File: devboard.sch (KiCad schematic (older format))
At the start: 95 parts, among them J1 Conn_01x04, J2 Conn_02x05_Odd_Even, J3 USB_B_Micro, J4 Conn_01x04, J5 Conn_02x10_Counter_Clockwise, J6 Conn_02x04_Counter_Clockwise, J7 Conn_02x03_Counter_Clockwise, Q1 Q_NPN_BEC, Q2 Q_NPN_BEC, SW1 SW_SPST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

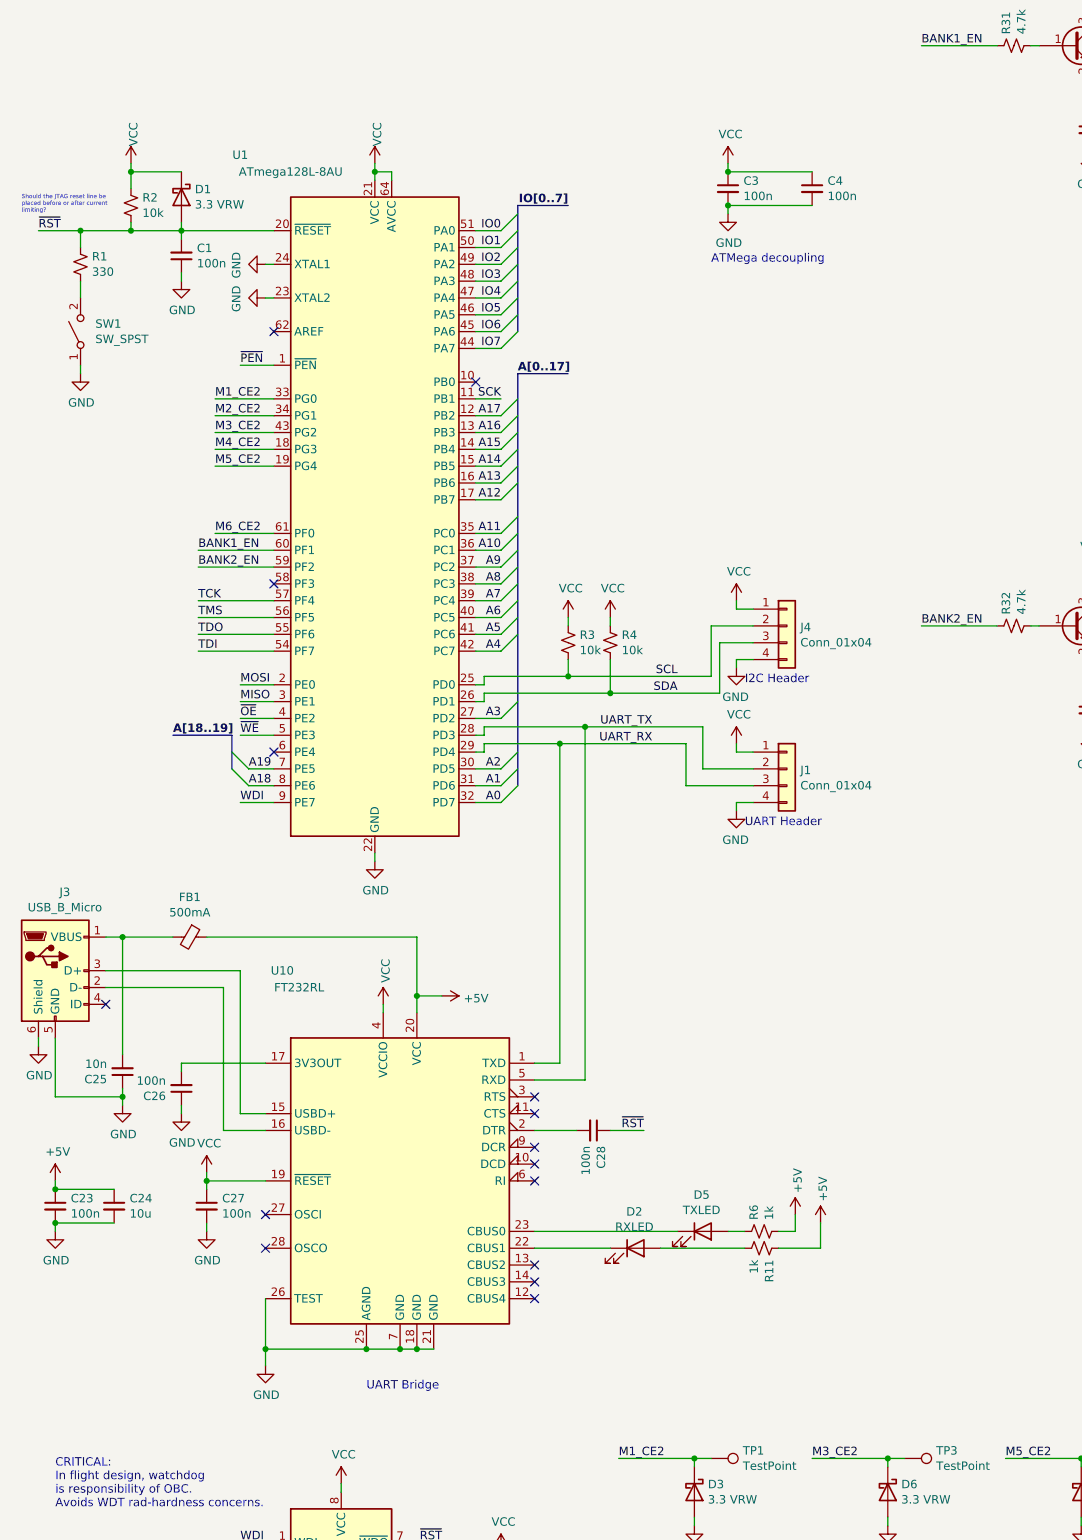
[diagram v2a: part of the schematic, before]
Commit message: Add crystal pads, MCU LED, fix serial routing
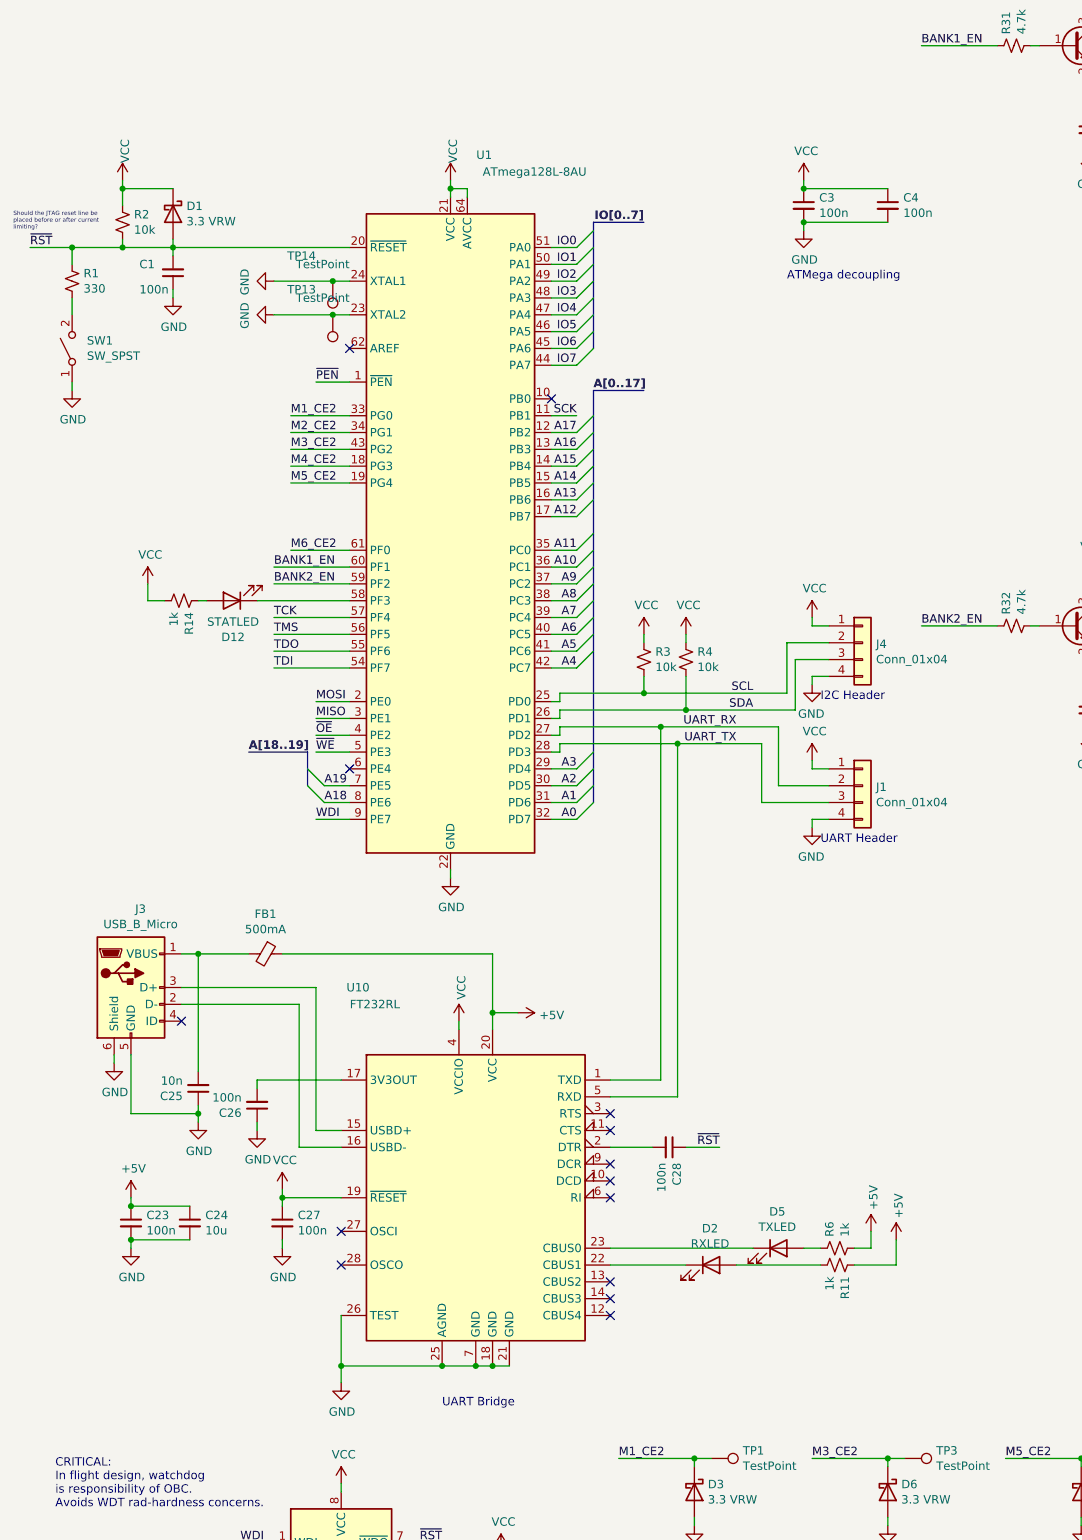
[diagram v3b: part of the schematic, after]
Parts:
- added D12: STATLED, LED_SMD:LED_0603_1608Metric_Castellated, symbol Device:LED
- added R14: 1k, Resistor_SMD:R_0603_1608Metric_Pad0.98x0.95mm_HandSolder, symbol Device:R_Small_US
- added TP13, TP14: TestPoint, TestPoint:TestPoint_Bridge_Pitch2.54mm_Drill0.7mm, symbol Connector:TestPoint
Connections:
- net A3: now also U1.29 (PD4); no longer U1.27 (PD2)
- net GND: now also TP13.1, TP14.1
- net UART_RX: now also J1.2 (Pin_2), U1.27 (PD2); no longer J1.3 (Pin_3), U1.29 (PD4)
- net UART_TX: now also J1.3 (Pin_3); no longer J1.2 (Pin_2)
- net VCC: now also R14.2
- net at U1.58 (PF3): now also D12.1 (K)
- new net: D12.2 (A), R14.1
- no-connect marks 17 -> 16
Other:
- moved on the sheet: C1, C23, C24, C25, C26, C27, C28, C3, C4, D1, D2, D5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

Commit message: Add more testpoints
Just in case the Cypress chip operates differently than advertised.
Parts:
- added TP15, TP16, TP19, TP20, TP21, TP22: TestPoint, TestPoint:TestPoint_Pad_D1.5mm, symbol Connector:TestPoint
- added TP17, TP18: TestPoint, Connector_PinHeader_2.54mm:PinHeader_1x01_P2.54mm_Vertical, symbol Connector:TestPoint
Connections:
- net ~OE: now also TP17.1
- net ~WE: now also TP18.1
- net at R5.2, U5.6 (~CE1): now also TP15.1
- net at R23.2, U6.6 (~CE1): now also TP19.1
- net at R27.2, U8.6 (~CE1): now also TP21.1
- net at R12.2, U3.6 (~CE1): now also TP16.1
- net at R24.2, U7.6 (~CE1): now also TP20.1
- net at R28.2, U9.6 (~CE1): now also TP22.1
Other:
- moved on the sheet: J5, J6
